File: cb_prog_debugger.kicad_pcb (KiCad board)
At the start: 2 copper layers, 35.6 x 35.6 mm, 49 parts, among them J1 USB_HOST, J2 Conn_01x03_Male, J3 USB_DEBUG, J4 Conn_02x03_Odd_Even, J5 ZIF16, U1 93LC56B, U2 LM1117-3.3, U3 CH341A, U4 FT232H, Y1 12 MHz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

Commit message: Set correct design rules
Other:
- net class Default: via_dia 0.6 -> 0.7; via_drill 0.4 -> 0.3
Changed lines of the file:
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@@
     (links 136)
     (no_connects 136)
-    (area 140.894999 85.014999 176.605001 120.725001)
+    (area 139.9 66.545 237.270002 149.86)
     (thickness 1.6)
     (drawings 4)
@@
     (segment_width 0.2)
     (edge_width 0.15)
-    (via_size 0.6)
-    (via_drill 0.4)
+    (via_size 0.7)
+    (via_drill 0.3)
     (via_min_size 0.4)
     (via_min_drill 0.3)
@@
     (clearance 0.2)
     (trace_width 0.2)
-    (via_dia 0.6)
-    (via_drill 0.4)
+    (via_dia 0.7)
+    (via_drill 0.3)
     (uvia_dia 0.3)
     (uvia_drill 0.1)

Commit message: Add differential net names
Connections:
- net Net-(J1-Pad2) renamed /USBHOST-
- net Net-(J1-Pad3) renamed /USBHOST+
- net Net-(J3-Pad2) renamed /USBDBG-
- net Net-(J3-Pad3) renamed /USBDBG+

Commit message: Fix shorted 3.3V-GND
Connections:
- C1 pad 2: +3V3 -> GND
- C10 pad 2: +3V3 -> GND
- C11 pad 2: +3V3 -> GND
- C12 pad 2: +3V3 -> GND
- C13 pad 2: +3V3 -> GND
- C14 pad 2: +3V3 -> GND
- C2 pad 2: +3V3 -> GND
- C3 pad 2: +3V3 -> GND
- C4 pad 2: +3V3 -> GND
- C5 pad 2: +3V3 -> GND
- C6 pad 2: +3V3 -> GND
- C7 pad 2: +3V3 -> GND
- C8 pad 2: +3V3 -> GND
- C9 pad 2: +3V3 -> GND
- D1 pad 1: +3V3 -> GND
- D2 pad 1: +3V3 -> GND
- J1 pad 5: +3V3 -> GND
- J1 pad 6: +3V3 -> GND
- J2 pad 1: +3V3 -> GND
- J3 pad 5: +3V3 -> GND
- J3 pad 6: +3V3 -> GND
- J4 pad 4: +3V3 -> /MOSI
- J4 pad 6: +3V3 -> GND
- J5 pad 1: +3V3 -> /MOSI
- J5 pad 12: +3V3 -> GND
- J5 pad 16: +3V3 -> GND
- R13 pad 1: +3V3 -> GND
- R15 pad 1: +3V3 -> GND
- R16 pad 1: +3V3 -> GND
- R17 pad 1: +3V3 -> GND
- R6 pad 2: +3V3 -> GND
- U1 pad 2: +3V3 -> GND
- U2 pad 1: +3V3 -> GND
- U3 pad 12: +3V3 -> GND
- U3 pad 20: +3V3 -> /MOSI
- U4 pad 10: +3V3 -> GND
- U4 pad 11: +3V3 -> GND
- U4 pad 22: +3V3 -> GND
- U4 pad 23: +3V3 -> GND
- U4 pad 35: +3V3 -> GND
- U4 pad 36: +3V3 -> GND
- U4 pad 4: +3V3 -> GND
- U4 pad 41: +3V3 -> GND
- U4 pad 42: +3V3 -> GND
- U4 pad 47: +3V3 -> GND
- U4 pad 48: +3V3 -> GND
- U4 pad 9: +3V3 -> GND

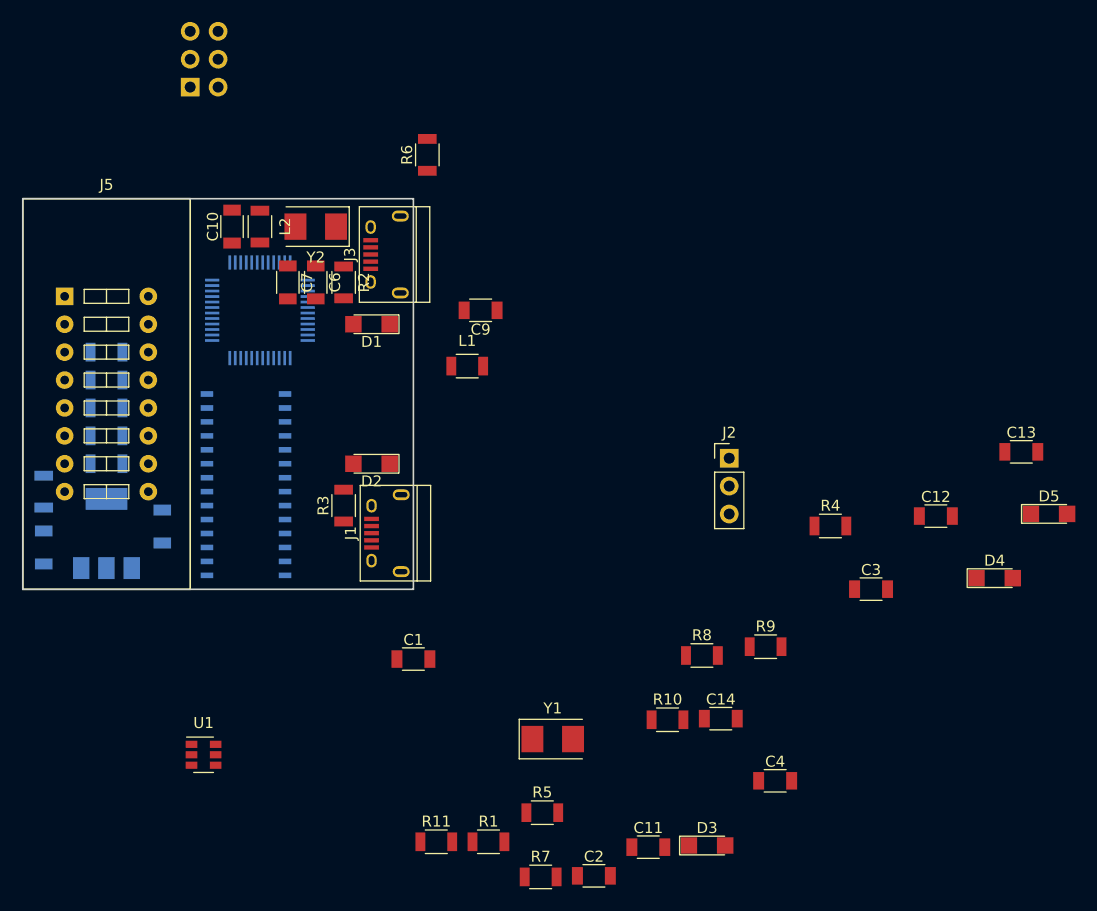
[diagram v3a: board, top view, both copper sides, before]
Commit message: Use 0805 packages
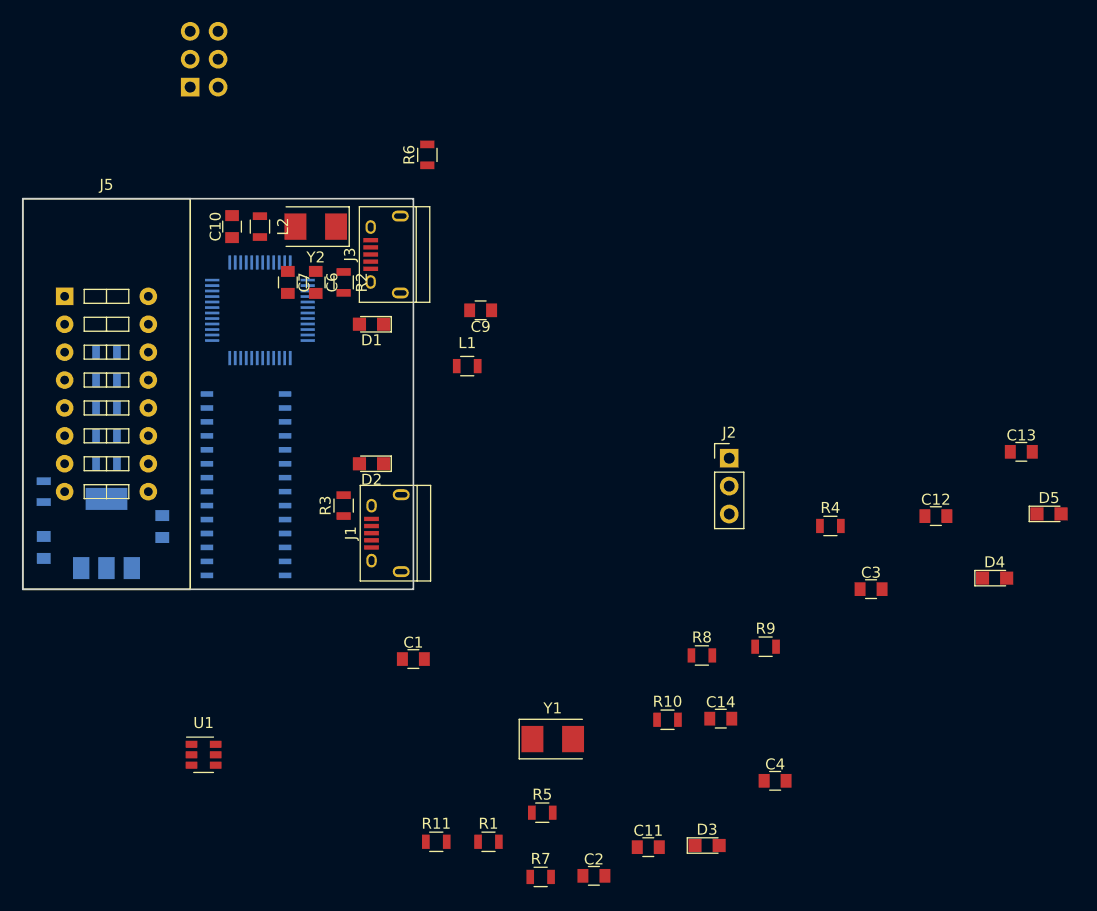
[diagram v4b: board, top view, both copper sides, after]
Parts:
- C1, C10, C11, C12, C13, C14, C2, C3, C4, C5, C6, C7, C8, C9: footprint Capacitors_SMD:C_1206 -> Capacitors_SMD:C_0805
- D1, D2, D3, D4, D5: footprint LEDs:LED_1206 -> LEDs:LED_0805
- L1, L2: footprint Inductors_SMD:L_1206 -> Inductors_SMD:L_0805
- R1, R10, R11, R12, R13, R14, R15, R16, R17, R2, R3, R4, R5, R6, R7, R8, R9: footprint Resistors_SMD:R_1206 -> Resistors_SMD:R_0805

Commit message: PCB: Add initial component layout
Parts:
- C1, C10, C11, C12, C13, C14, C2, C3, C4, C6, C7, C9, L1, L2, R4, U1, Y1, Y2: moved to B.Cu
- moved C13 74.2 mm to (158.1, 100.3), turned to 270 degrees
- moved D5 73.9 mm to (161.0, 104.9), turned to 180 degrees
- moved C4 72.9 mm to (157.5, 87.0), turned to 270 degrees
- moved R4 69.9 mm to (148.8, 90.9), turned to 180 degrees
- moved D4 69.4 mm to (161.0, 108.2), turned to 180 degrees
- moved C12 69.1 mm to (155.2, 108.2), turned to 90 degrees
- moved C3 66.4 mm to (161.3, 86.4)
- moved C2 63.8 mm to (154.9, 95.5), turned to 180 degrees
- moved C14 59.3 mm to (166.4, 87.0), turned to 270 degrees
- moved R5 59.0 mm to (159.4, 89.5), turned to 90 degrees
- moved C11 55.1 mm to (164.5, 100.3), turned to 270 degrees
- moved R8 54.3 mm to (159.4, 94.0), turned to 90 degrees
- moved R9 53.8 mm to (157.7, 108.5), turned to 90 degrees
- moved D3 53.0 mm to (160.8, 112.3), turned to 180 degrees
- moved Y1 48.6 mm to (154.9, 99.8), turned to 90 degrees
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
